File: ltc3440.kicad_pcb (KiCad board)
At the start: 2 copper layers, 22.9 x 17 mm, 10 parts, among them J1 Conn_01x04, U1 LTC3440EDD

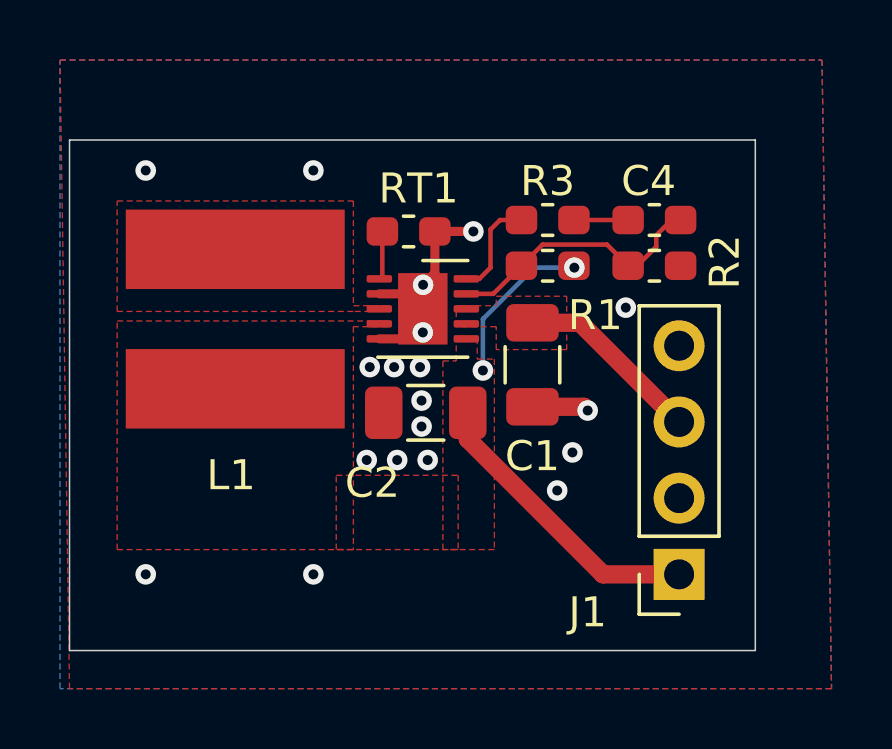
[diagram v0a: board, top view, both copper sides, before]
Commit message: add inductor 3d model and adjust cu pours
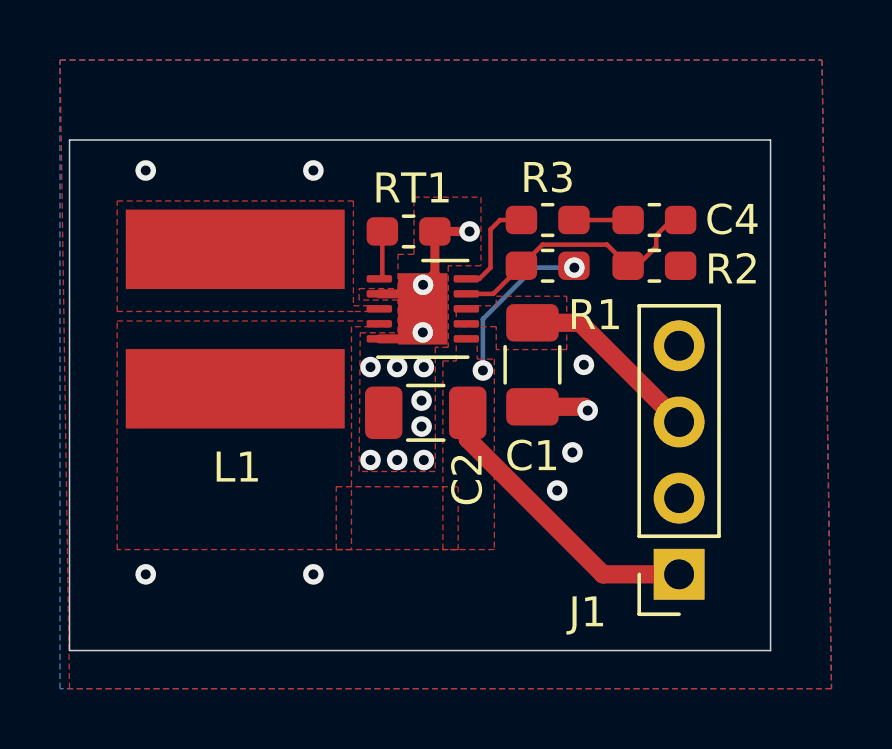
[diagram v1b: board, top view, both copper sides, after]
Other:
- board size 22.9 x 17 mm -> 23.4 x 17 mm

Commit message: change to burst mode
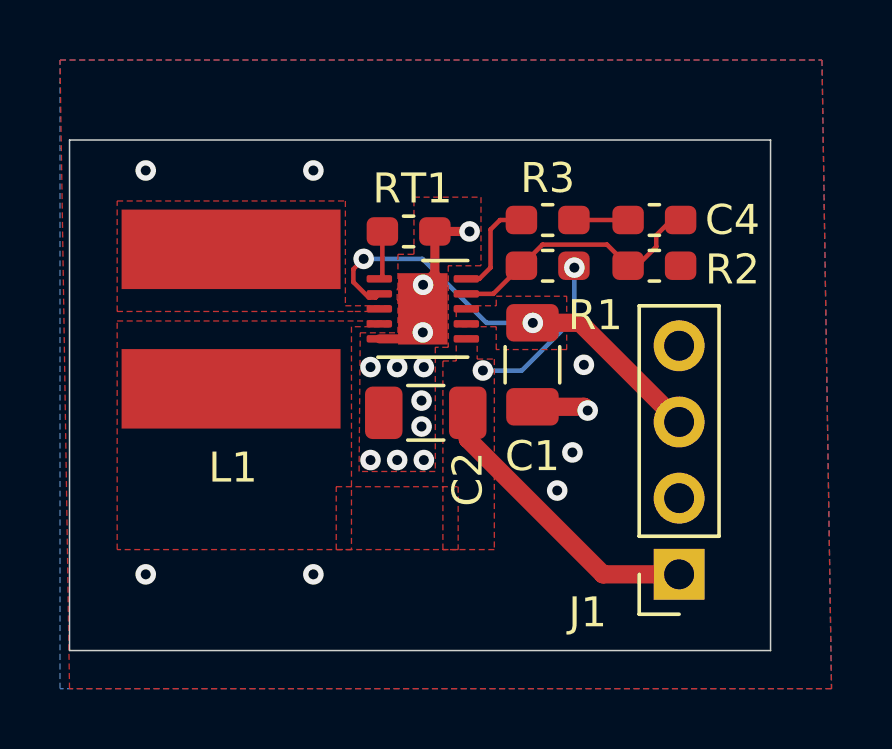
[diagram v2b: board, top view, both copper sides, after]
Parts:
- moved L1 0.14 mm to (159.1, 107.1)
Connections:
- U1 pad 2: GND -> +BATT
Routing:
- net +BATT: track 6.26 -> 14.8 mm, vias 0 -> 2
- net GND: track 8.13 -> 6.97 mm

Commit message: change inductor with smaller footprint
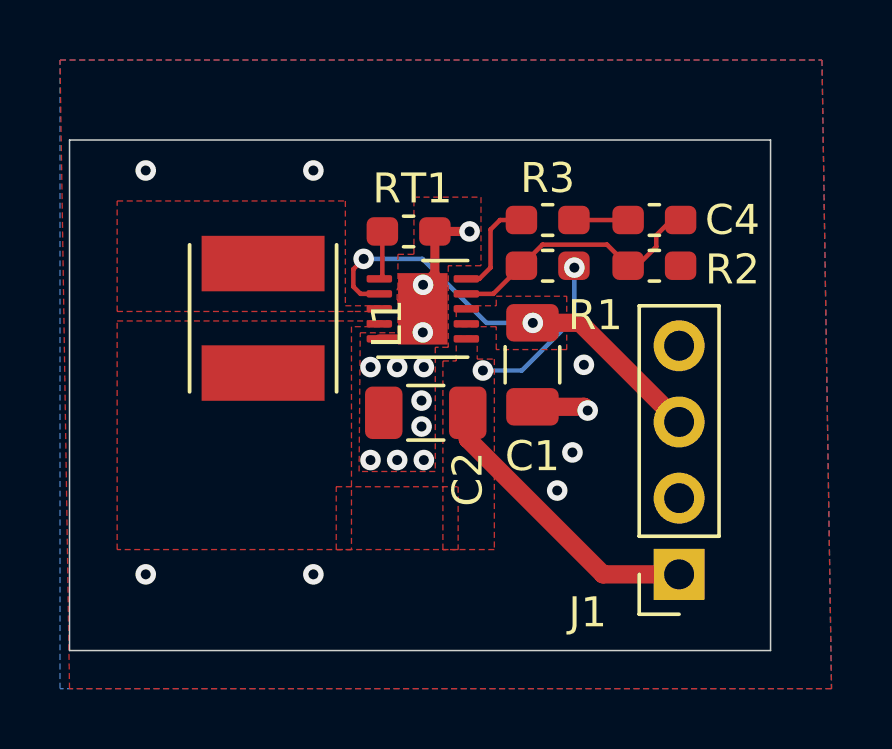
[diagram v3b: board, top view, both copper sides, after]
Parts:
- L1: footprint ltc3440:L_Sumida-CDRH6D38 -> ltc3440:IND_LQH5BPN100M38L
- moved L1 1.07 mm to (160.1, 107.0), turned to 270 degrees

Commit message: fix error sw2 to vout
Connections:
- L1 pad 2: +3V3 -> Net-(L1-Pad2)
- U1 pad 4: +3V3 -> Net-(L1-Pad2)
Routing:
- added copper zone on F.Cu, net Net-(L1-Pad2)

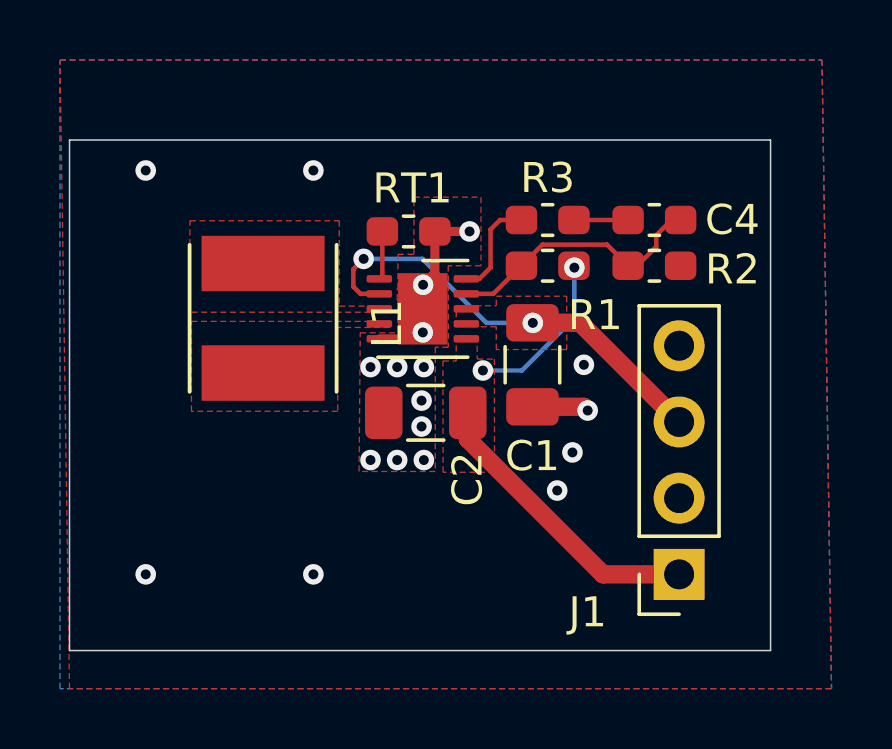
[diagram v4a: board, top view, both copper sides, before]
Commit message: reduce board size
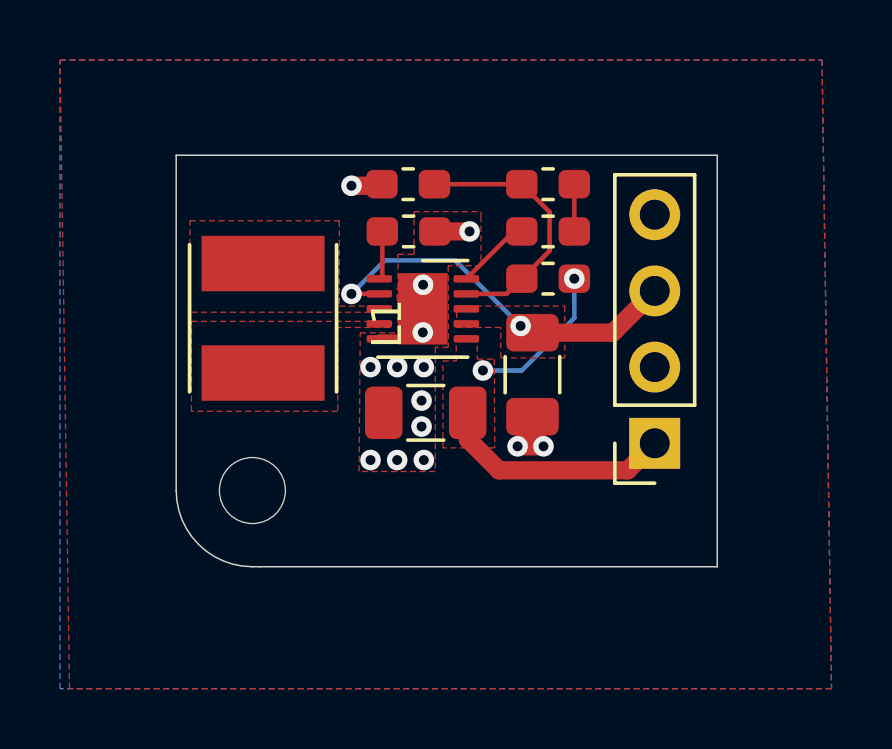
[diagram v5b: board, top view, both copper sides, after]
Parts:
- added H1: MountingHole_Pad, MountingHole:MountingHole_2.2mm_M2, F.Cu at (159.8, 112.8)
- moved R2 8.64 mm to (165.0, 102.6), turned to 180 degrees
- moved J1 4.44 mm to (173.2, 111.2)
- moved C4 3.74 mm to (169.6, 102.6), turned to 180 degrees
- moved R1 0.43 mm to (169.6, 105.7)
- moved R3 0.38 mm to (169.6, 104.1)
- moved C1 0.33 mm to (169.1, 108.9)
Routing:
- net +3V3: track 15.2 -> 13.0 mm
- net +BATT: track 14.8 -> 12.6 mm
- net GND: track 6.97 -> 8.52 mm, vias 19 -> 14
- net Net-(R3-Pad2): track 3.39 -> 2.50 mm
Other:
- board size 23.4 x 17 mm -> 18 x 13.7 mm
